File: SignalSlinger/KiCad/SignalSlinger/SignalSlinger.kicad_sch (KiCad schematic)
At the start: 61 parts, among them J101 Conn_01x02, J102 Conn_01x02, J103 Conn_01x02, J104 Conn_01x02, J105 Conn_01x02, J106 Conn_01x02, J107 DB9 Female, J108 Conn_01x02, J109 Conn_01x03, J110 Conn_01x02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

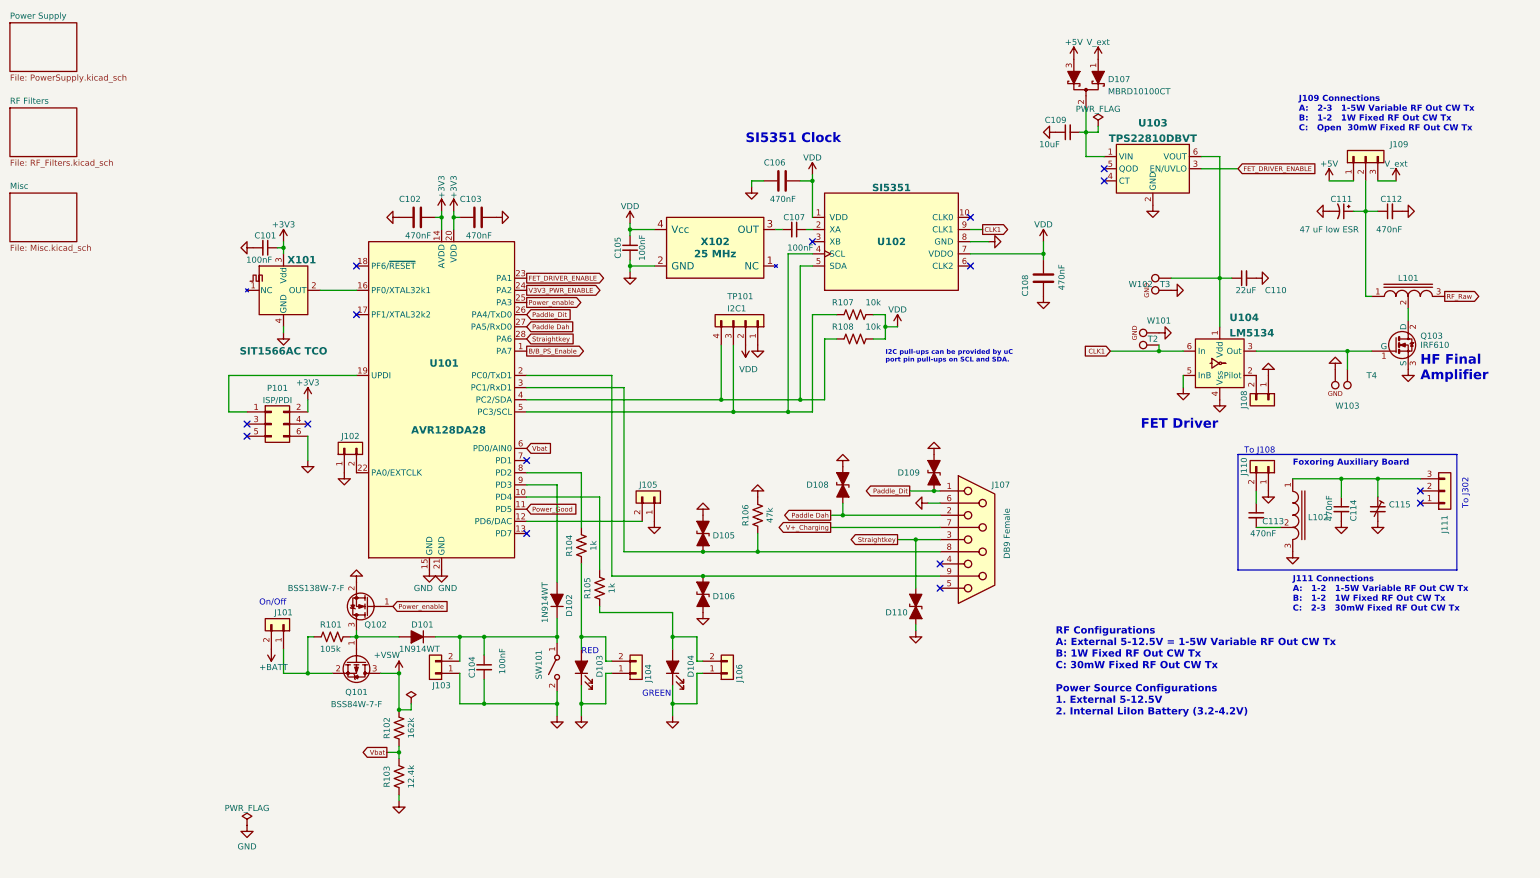
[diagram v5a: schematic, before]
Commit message: PCB Development
Added fan control circuit
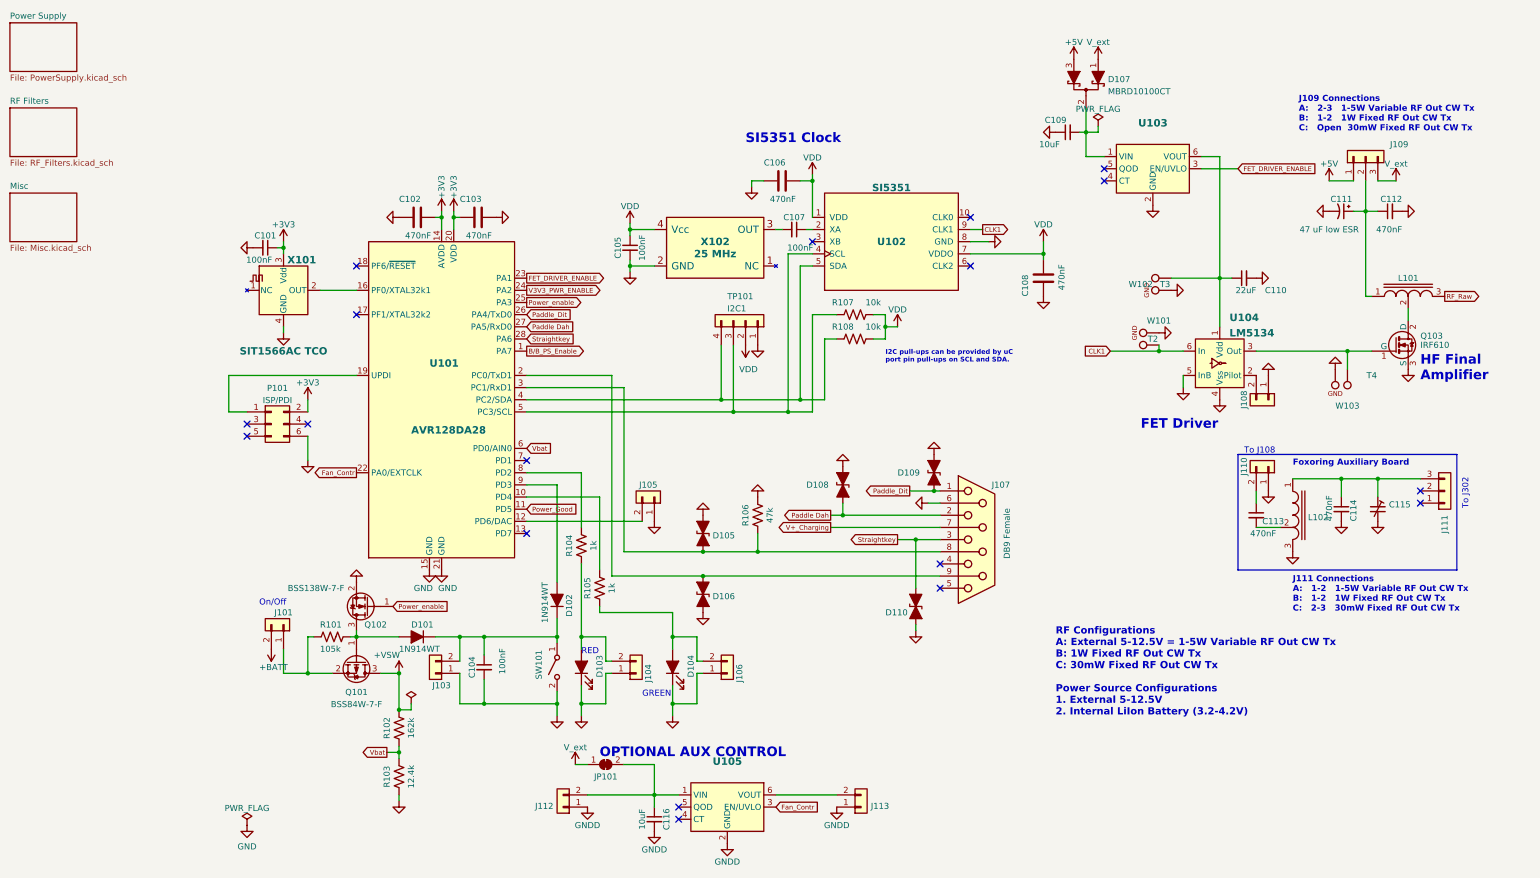
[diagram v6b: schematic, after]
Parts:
- removed J102: Conn_01x02, Connector_PinSocket_2.54mm:PinSocket_1x02_P2.54mm_Vertical, symbol Connector_Generic:Conn_01x02
- added C116: 10uF, Capacitor_SMD:C_0805_2012Metric, symbol Device:C_Small
- added J112, J113: (no value), symbol Connector_Generic:Conn_01x02
- added JP101: (no value), Jumper:SolderJumper-2_P1.3mm_Bridged_RoundedPad1.0x1.5mm, symbol Jumper:SolderJumper_2_Bridged
- added U105: (no value), symbol Power_Management:TPS22810DBVT
- D103: value (none) -> Red LED; footprint (none) -> LED_SMD:LED_0805_2012Metric
- D104: value (none) -> Green LED; footprint (none) -> LED_SMD:LED_APDA1806SECK
- U103: value TPS22810DBVT -> (none); footprint TO_SOT_Packages_SMD:SOT-23-6 -> (none)
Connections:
- net GND: now also C116.2, J112.1 (Pin_1), J113.1 (Pin_1), U105.2 (GND)
- net V_ext: now also JP101.1 (A)
- net Fan_Contr: now reaches U101.22 (PA0/EXTCLK)
- net Fan_Contr: now also U105.3 (EN/UVLO)
- new net: J113.2 (Pin_2), U105.6 (VOUT)
- new net: C116.1, J112.2 (Pin_2), JP101.2 (B), U105.1 (VIN)
- no-connect marks 16 -> 18
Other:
- note added: "OPTIONAL AUX CONTROL"

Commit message: PCB Development
More updates
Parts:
- J112: value (none) -> External Power Source; footprint (none) -> Connector_PinHeader_2.54mm:PinHeader_1x02_P2.54mm_Vertical
- J113: value (none) -> Controlled Power; footprint (none) -> Connector_PinHeader_2.54mm:PinHeader_1x02_P2.54mm_Vertical
- JP101: value (none) -> V-ext disable
- U103: Link <a href="https://www.digikey.com/products/en?keywords=296-4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 -> https://www.digikey.com/products/en?keywords=296-45304-1-ND
- U105: value (none) -> TPS22810DBVT; footprint (none) -> Package_TO_SOT_SMD:SOT-23-6
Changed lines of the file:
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@@
     (effects (font (size 2.0066 2.0066) (thickness 0.4013) bold) (justify left bottom))
   )
-  (text "OPTIONAL AUX CONTROL" (at 95.25 171.45 0)
+  (text "OPTIONAL AUX CONTROL" (at 101.6 170.18 0)
     (effects (font (size 2.0066 2.0066) (thickness 0.4013) bold) (justify left bottom))
   )
@@
       (effects (font (size 1.27 1.27)) (justify left))
     )
-    (property "Value" "" (id 1) (at 147.32 175.26 0)
-      (effects (font (size 1.27 1.27)) (justify left))
-    )
-    (property "Footprint" "" (id 2) (at 149.86 181.61 0)
+    (property "Value" "Controlled Power" (id 1) (at 147.32 175.26 0)
+      (effects (font (size 1.27 1.27)) (justify left))
+    )
+    (property "Footprint" "Connector_PinHeader_2.54mm:PinHeader_1x02_P2.54mm_Vertical" (id 2) (at 149.86 181.61 0)
       (effects (font (size 1.27 1.27)) hide)
     )
@@
       (effects (font (size 1.27 1.27)) hide)
     )
-    (property "Link" "<a href=\"https://www.digikey.com/products/en?keywords=296-45304-1-ND\">Link</a>" (id 5) (at 210.82 48.26 0)
+    (property "Link" "https://www.digikey.com/products/en?keywords=296-45304-1-ND" (id 5) (at 210.82 48.26 0)
       (effects (font (size 1.27 1.27)) hide)
     )
@@
       (effects (font (size 1.27 1.27)) (justify left))
     )
-    (property "Value" "" (id 1) (at 85.09 179.07 0)
-      (effects (font (size 1.27 1.27)) (justify left))
-    )
-    (property "Footprint" "" (id 2) (at 87.63 181.61 0)
+    (property "Value" "External Power Source" (id 1) (at 85.09 179.07 0)
+      (effects (font (size 1.27 1.27)) (justify left))
+    )
+    (property "Footprint" "Connector_PinHeader_2.54mm:PinHeader_1x02_P2.54mm_Vertical" (id 2) (at 87.63 181.61 0)
       (effects (font (size 1.27 1.27)) hide)
     )
@@
       (effects (font (size 1.5494 1.5494) bold))
     )
-    (property "Value" "" (id 1) (at 121.92 175.2859 0)
+    (property "Value" "TPS22810DBVT" (id 1) (at 121.92 175.2859 0)
       (effects (font (size 1.5494 1.5494) bold))
     )
-    (property "Footprint" "" (id 2) (at 121.92 199.39 0)
+    (property "Footprint" "Package_TO_SOT_SMD:SOT-23-6" (id 2) (at 121.92 199.39 0)
       (effects (font (size 1.27 1.27)) hide)
     )
@@
     (in_bom yes) (on_board yes)
     (property "Reference" "JP101" (id 0) (at 96.52 175.26 0))
-    (property "Value" "" (id 1) (at 99.06 176.53 0))
+    (property "Value" "V-ext disable" (id 1) (at 99.06 176.53 0))
     (property "Footprint" "Jumper:SolderJumper-2_P1.3mm_Bridged_RoundedPad1.0x1.5mm" (id 2) (at 96.52 172.72 0)
       (effects (font (size 1.27 1.27)) hide)

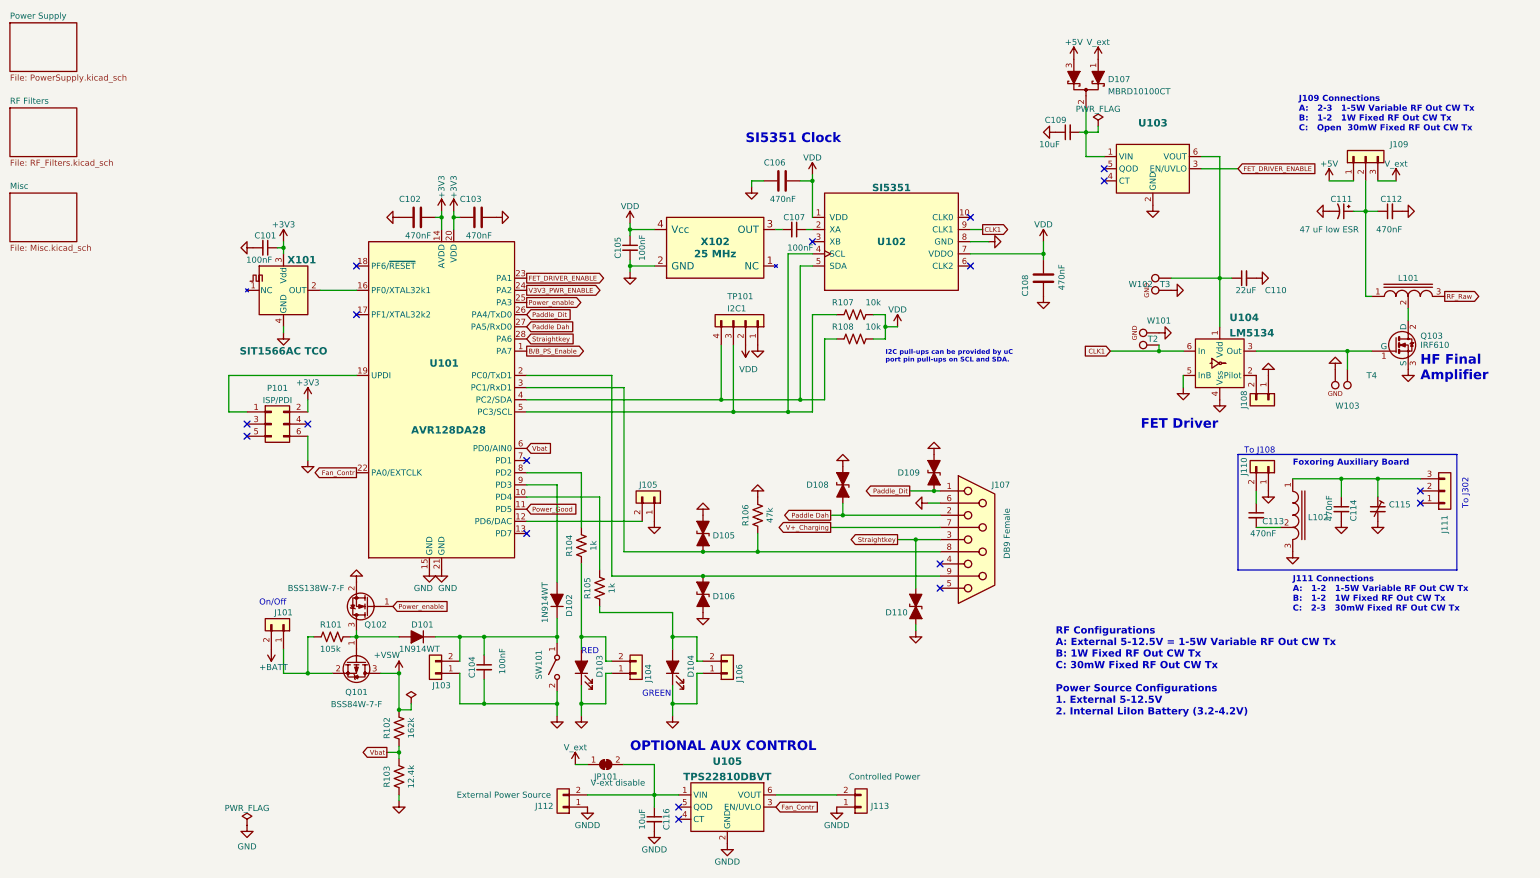
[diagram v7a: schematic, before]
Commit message: BOM
Updates to BOM parts
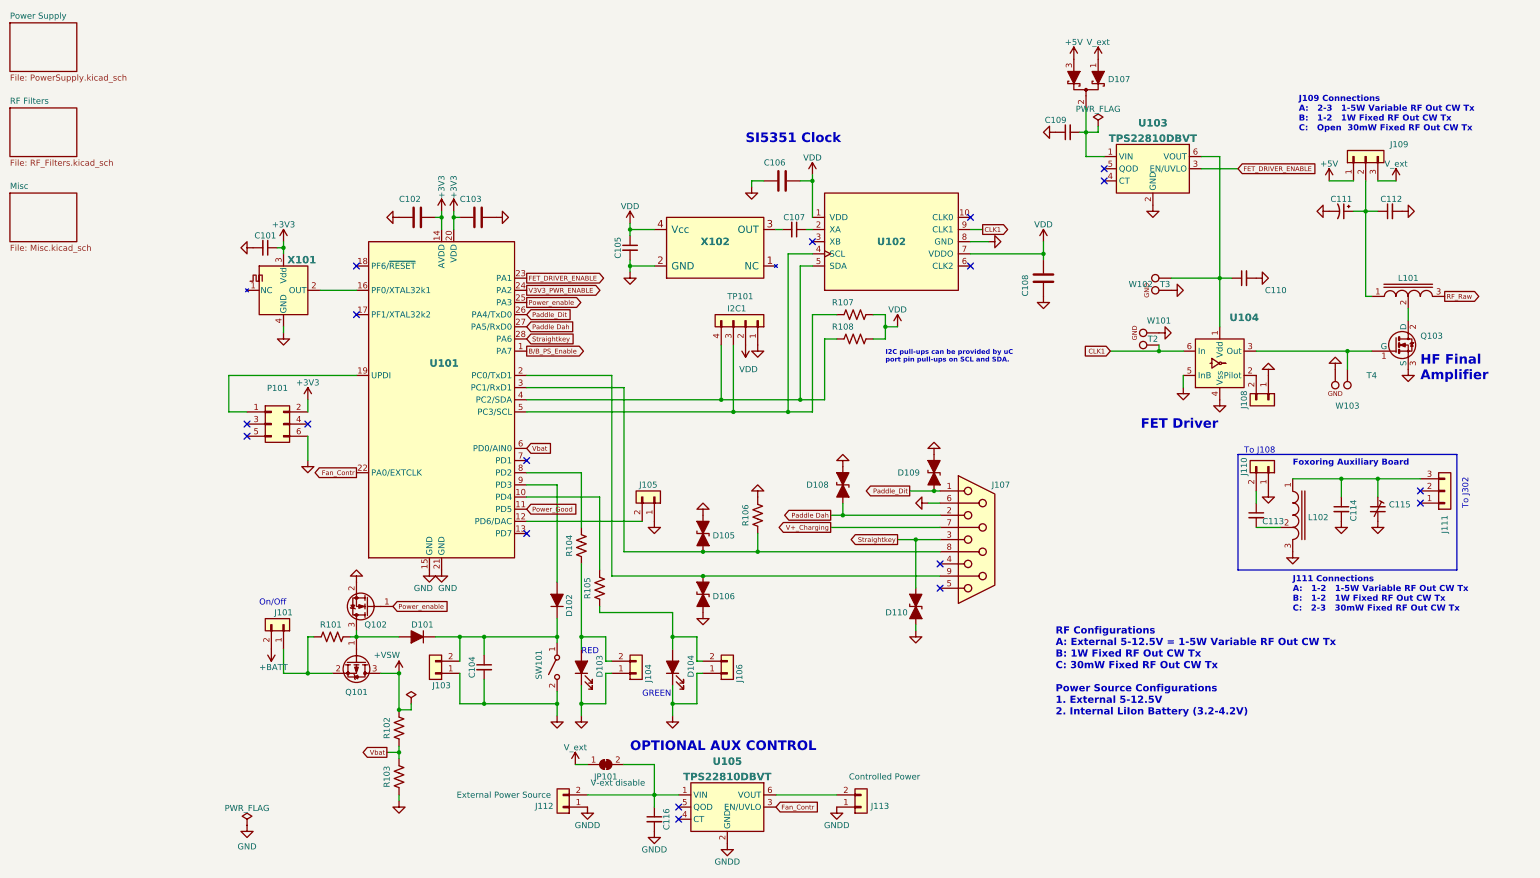
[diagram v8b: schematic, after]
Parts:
- C101, C104, C105, C107: value 100nF -> (none); footprint Capacitor_SMD:C_0805_2012Metric -> (none); LCSC Part Number (none) -> C29926; Link (none) -> https://www.digikey.com/short/q2f22qnq
- C102, C103, C106, C108, C112, C113, C114: value 470nF -> (none); footprint Capacitor_SMD:C_0805_2012Metric -> (none); Link <a href="https://www.digikey.com/products/en?keywords=478-9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 -> https://www.digikey.com/products/en?keywords=478-9924-1-ND
- C109, C116: value 10uF -> (none); footprint Capacitor_SMD:C_0805_2012Metric -> (none); Digi-Key Part No. 1276-1764-1-ND -> 445-14418-1-ND; LCSC Part Number (none) -> C3843628; Link (none) -> https://www.digikey.com/short/p8qdn4mp; Manufacturer Samsung Electro-Mechanics -> TDK Corporation; Manufacturer PN CL21B106KPQNNNE -> C2012X5R1V106K125AC
- C110: value 22uF -> (none); footprint Capacitor_SMD:C_1210_3225Metric -> (none); Link <a href="https://www.digikey.com/products/en?keywords=1276-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 -> https://www.digikey.com/products/en?keywords=1276-3373-1-ND
- C111: value 47 uF low ESR -> (none); footprint Capacitors:C_2917 -> (none); Link <a href="https://www.digikey.com/products/en?keywords=399-3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 -> https://www.digikey.com/products/en?keywords=399-3904-1-ND
- C115: value C_Trim_Small -> (none); footprint Capacitors:MURATA-TZC3 -> (none)
- D101, D102: value 1N914WT -> (none); footprint Diode_SMD:D_SOD-523 -> (none); LCSC Part Number (none) -> C83482
- D103: value Red LED -> (none); footprint LED_SMD:LED_0805_2012Metric -> (none); LCSC Part Number (none) -> C94868
- D104: value Green LED -> (none); footprint LED_SMD:LED_APDA1806SECK -> (none); LCSC Part Number (none) -> C98221
- D105, D106, D108, D109, D110: value ESD9B5.0ST5G_1 -> (none); footprint Diode_SMD:D_0603_1608Metric -> (none); Link <a href="https://www.digikey.com/products/en?keywords=CG060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 -> https://www.digikey.com/products/en?keywords=CG0603MLC-05LE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
- D107: value MBRD10100CT -> (none); footprint Package_TO_SOT_SMD:TO-252-2 -> (none); LCSC Part Number (none) -> C156323
- J107: value DB9 Female -> (none); footprint Connector_Dsub:DSUB-9_Female_EdgeMount_P2.77mm -> (none); Link <a href="https://www.digikey.com/products/en?keywords=609-1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 -> https://www.digikey.com/products/en?keywords=609-1525-ND
- L101: value 9T #24 Bifilar T50-43 -> (none); footprint Inductors:Toroid_T-50A_TH_BF_CT -> (none); Link <a href="http://www.amidoncorp.com/ft-50A-43/">Link</a> -> http://www.amidoncorp.com/ft-50A-43/
- L102: value INDUCTOR_tapped -> (none); footprint Inductors:Toroid_T-50A_TH_BF_CT_Vertical -> (none); Link <a href="http://www.amidoncorp.com/ft-50A-43/">Link</a> -> http://www.amidoncorp.com/ft-50A-43/
- P101: value ISP/PDI -> (none); footprint Connector_PinHeader_2.54mm:PinHeader_2x03_P2.54mm_Vertical_SMD -> (none); LCSC Part Number (none) -> C178294; Link <a href="https://www.digikey.com/products/en?keywords=609-3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 -> https://www.digikey.com/products/en?keywords=609-3487-1-ND
- Q101: value BSS84W-7-F -> (none); footprint Package_TO_SOT_SMD:SOT-323_SC-70 -> (none); LCSC Part Number (none) -> C110490; Link (none) -> https://www.digikey.com/short/fjvhfm07
- Q102: value BSS138W-7-F -> (none); footprint Package_TO_SOT_SMD:SOT-323_SC-70 -> (none); LCSC Part Number (none) -> C24553; Link (none) -> https://www.digikey.com/short/m8f8nn79
- Q103: value IRF610 -> (none); footprint TO_SOT_Packages:TO-220_Neutral123_Vertical_LargePads -> (none); Link <a href="https://www.digikey.com/products/en?keywords=IRF61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 -> https://www.digikey.com/products/en?keywords=IRF610PBF-ND
- R101: value 105k -> (none); footprint Resistor_SMD:R_0805_2012Metric -> (none); LCSC Part Number (none) -> C273877
- R102: value 162k -> (none); footprint Resistor_SMD:R_0805_2012Metric -> (none); LCSC Part Number (none) -> C273888
- R103: value 12.4k -> (none); footprint Resistor_SMD:R_0805_2012Metric -> (none); LCSC Part Number (none) -> C137595
- R104, R105: value 1k -> (none); footprint Resistor_SMD:R_0805_2012Metric -> (none); LCSC Part Number (none) -> C17513
- R106: value 47k -> (none); footprint Resistor_SMD:R_0805_2012Metric -> (none); LCSC Part Number (none) -> C126351
- R107, R108: value 10k -> (none); footprint Capacitor_SMD:C_0805_2012Metric -> (none); LCSC Part Number (none) -> C2441435
- U101: value AVR128DA28 -> (none); footprint Package_SO:SOIC-28W_7.5x17.9mm_P1.27mm -> (none); LCSC Part Number (none) -> C1870730; Link (none) -> https://www.digikey.com/short/781hqp8f
- U102: value SI5351 -> (none); footprint Package_SO:MSOP-10_3x3mm_P0.5mm -> (none); Link <a href="https://www.digikey.com/products/en?keywords=336-2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 -> https://www.digikey.com/products/en?keywords=336-2399-5-ND
- U103: value (none) -> TPS22810DBVT; footprint (none) -> Package_TO_SOT_SMD:SOT-23-6
- U104: value LM5134 -> (none); footprint Package_TO_SOT_SMD:SOT-23-6-LM5134 -> (none); Link <a href="https://www.digikey.com/products/en?keywords=296-4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 -> https://www.digikey.com/products/en?keywords=296-40244-1-ND
- X101: value SIT1566AC TCO -> (none); footprint Oscillator:Oscillator_SMD_SiTime_SIT1566AC-4Pin_BGA -> (none); Link (none) -> https://www.digikey.com/short/r7q3vdbp
- X102: value 25 MHz -> (none); footprint Crystal:Crystal_SMD_TXETCLSANF-4Pin -> (none); Link <a href="https://www.digikey.com/products/en?keywords=1664-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 -> https://www.digikey.com/products/en?keywords=1664-1273-1-ND
